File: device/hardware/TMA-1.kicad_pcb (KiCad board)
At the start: 2 copper layers, 143.8 x 129.5 mm, 72 parts, among them J1 MAIN I/O, J2 I2C, Q1 2N3904, Q2 2N3904, Q3 2N3904, Q4 2N3904, Q5 2N3904, Q6 2N3904, Q7 2N3904, Q8 2N3904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

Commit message: improve: pin name silkscreen
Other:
- board text added: "AIN0"
- board text added: "AIN1"
- board text added: "AIN2"
- board text added: "AIN3"
- board text added: "CANH"
- board text added: "CANL"
- board text added: "DIN0"
- board text added: "DIN1"
- board text added: "DIN2"
- board text added: "DIN3"
- board text added: "DIN4"
- board text added: "DIN5"
- board text added: "DIN6"
- board text added: "DIN7"
- board text added: "DRX"
- board text added: "DTX"
- board text added: "GND"
- board text added: "LRX"
- board text added: "LTX"
- board text added: "PIN0"
- board text added: "PIN1"
- board text added: "PIN2"
- board text added: "PIN3"
- board text added: "SCL"
- board text added: "SDA"
- board text added: "VIN"
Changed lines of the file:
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@@
   (gr_line (start 216.408 35.687) (end 216.408 153.035)
     (stroke (width 0.1) (type default)) (layer "Edge.Cuts"))
+  (gr_text "DIN6" (at 175.768 44.577) (layer "B.SilkS")
+    (effects (font (size 1 1) (thickness 0.15)) (justify left bottom mirror))
+  )
+  (gr_text "PIN2" (at 192.532 44.577) (layer "B.SilkS")
+    (effects (font (size 1 1) (thickness 0.15)) (justify left bottom mirror))
+  )
+  (gr_text "PIN1" (at 188.341 56.642) (layer "B.SilkS")
+    (effects (font (size 1 1) (thickness 0.15)) (justify left bottom mirror))
+  )
+  (gr_text "LTX" (at 200.406 44.577) (layer "B.SilkS")
+    (effects (font (size 1 1) (thickness 0.15)) (justify left bottom mirror))
+  )
+  (gr_text "DIN7" (at 175.895 56.642) (layer "B.SilkS")
+    (effects (font (size 1 1) (thickness 0.15)) (justify left bottom mirror))
+  )
+  (gr_text "DIN5" (at 171.577 56.642) (layer "B.SilkS")
+    (effects (font (size 1 1) (thickness 0.15)) (justify left bottom mirror))
+  )
+  (gr_text "DIN1" (at 163.068 56.642) (layer "B.SilkS")
+    (effects (font (size 1 1) (thickness 0.15)) (justify left bottom mirror))
+  )
+  (gr_text "CANL" (at 205.359 56.642) (layer "B.SilkS")
+    (effects (font (size 1 1) (thickness 0.15)) (justify left bottom mirror))
+  )
+  (gr_text "DIN0" (at 163.068 44.577) (layer "B.SilkS")
+    (effects (font (size 1 1) (thickness 0.15)) (justify left bottom mirror))
+  )
+  (gr_text "SDA" (at 211.836 93.472) (layer "B.SilkS")
+    (effects (font (size 1 1) (thickness 0.15)) (justify left bottom mirror))
+  )
+  (gr_text "DRX" (at 196.469 56.642) (layer "B.SilkS")
+    (effects (font (size 1 1) (thickness 0.15)) (justify left bottom mirror))
+  )
+  (gr_text "AIN3" (at 184.15 56.642) (layer "B.SilkS")
+    (effects (font (size 1 1) (thickness 0.15)) (justify left bottom mirror))
+  )
+  (gr_text "AIN2" (at 184.15 44.577) (layer "B.SilkS")
+    (effects (font (size 1 1) (thickness 0.15)) (justify left bottom mirror))
+  )
+  (gr_text "DIN3" (at 167.259 56.642) (layer "B.SilkS")
+    (effects (font (size 1 1) (thickness 0.15)) (justify left bottom mirror))
+  )
+  (gr_text "VIN" (at 158.242 44.577) (layer "B.SilkS")
+    (effects (font (size 1 1) (thickness 0.15)) (justify left bottom mirror))
+  )
+  (gr_text "DIN4" (at 171.577 44.577) (layer "B.SilkS")
+    (effects (font (size 1 1) (thickness 0.15)) (justify left bottom mirror))
+  )
+  (gr_text "DTX" (at 196.469 44.577) (layer "B.SilkS")
+    (effects (font (size 1 1) (thickness 0.15)) (justify left bottom mirror))
+  )
+  (gr_text "GND" (at 158.75 56.642) (layer "B.SilkS")
+    (effects (font (size 1 1) (thickness 0.15)) (justify left bottom mirror))
+  )
+  (gr_text "PIN3" (at 192.532 56.642) (layer "B.SilkS")
+    (effects (font (size 1 1) (thickness 0.15)) (justify left bottom mirror))
+  )
+  (gr_text "DIN2" (at 167.259 44.577) (layer "B.SilkS")
+    (effects (font (size 1 1) (thickness 0.15)) (justify left bottom mirror))
+  )
+  (gr_text "AIN1" (at 179.959 56.642) (layer "B.SilkS")
+    (effects (font (size 1 1) (thickness 0.15)) (justify left bottom mirror))
+  )
+  (gr_text "AIN0" (at 179.959 44.577) (layer "B.SilkS")
+    (effects (font (size 1 1) (thickness 0.15)) (justify left bottom mirror))
+  )
+  (gr_text "CANH" (at 205.359 44.577) (layer "B.SilkS")
+    (effects (font (size 1 1) (thickness 0.15)) (justify left bottom mirror))
+  )
+  (gr_text "LRX" (at 200.533 56.642) (layer "B.SilkS")
+    (effects (font (size 1 1) (thickness 0.15)) (justify left bottom mirror))
+  )
+  (gr_text "SCL" (at 211.836 86.487) (layer "B.SilkS")
+    (effects (font (size 1 1) (thickness 0.15)) (justify left bottom mirror))
+  )
+  (gr_text "PIN0" (at 188.341 44.577) (layer "B.SilkS")
+    (effects (font (size 1 1) (thickness 0.15)) (justify left bottom mirror))
+  )
   (gr_text "PULSE" (at 176.911 146.05) (layer "F.SilkS")
     (effects (font (size 1.27 1.27) (thickness 0.254) bold) (justify left bottom))

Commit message: improve: PCB v1.1 add debug uart jumper
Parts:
- J2: value I2C -> DEBUG UART; footprint Connector_Molex:Molex_SPOX_5267-02A_1x02_P2.50mm_Vertical -> Connector_PinHeader_2.54mm:PinHeader_1x03_P2.54mm_Vertical
- U2: value NodeMCU-32S -> NODEMCU32S
- moved J2 4.03 mm to (210.7, 86.5), turned to 0 degrees
- renumbered C2 to C1
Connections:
- J1 pad 10: /DEBUG_UART_TX -> /LOG_UART_TX
- J1 pad 11: /LOG_UART_TX -> /ESP_I2C_SDA
- J1 pad 22: /DEBUG_UART_RX -> /LOG_UART_RX
- J1 pad 23: /LOG_UART_RX -> /ESP_I2C_SCL
- J2 pad 1: /ESP_I2C_SDA -> /DEBUG_UART_TX
- J2 pad 2: /ESP_I2C_SCL -> /DEBUG_UART_RX
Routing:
- net /DEBUG_UART_RX: track 190.2 -> 233.4 mm
- net /ESP_I2C_SDA: track 222.0 -> 264.8 mm
- net /DEBUG_UART_TX: track 174.9 -> 217.4 mm
- net /ESP_I2C_SCL: track 216.1 -> 248.7 mm
- net /LOG_UART_RX: track 198.1 -> 196.2 mm
- net /LOG_UART_TX: track 191.8 -> 190.0 mm
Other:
- board text added: "Monolith TMA-1 Datalogger v1.1"
- board text added: "RX"
- board text added: "TX"
- board text removed: "DRX"
- board text removed: "DTX"
- board text removed: "Monolith TMA-1 Datalogger v1.0"

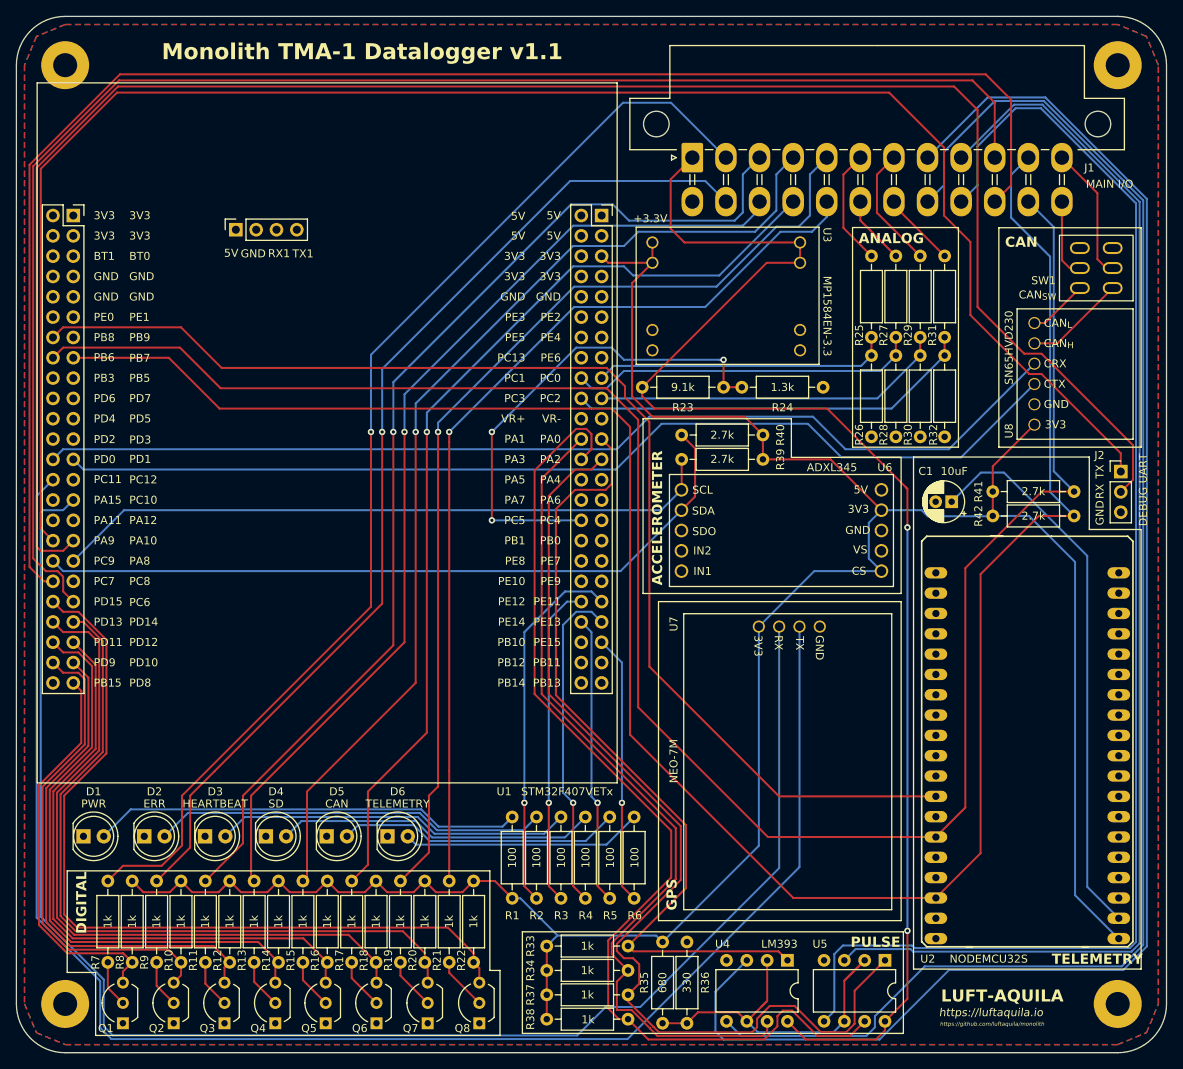
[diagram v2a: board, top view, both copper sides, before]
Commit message: fix: misc bugs PCB v1.2
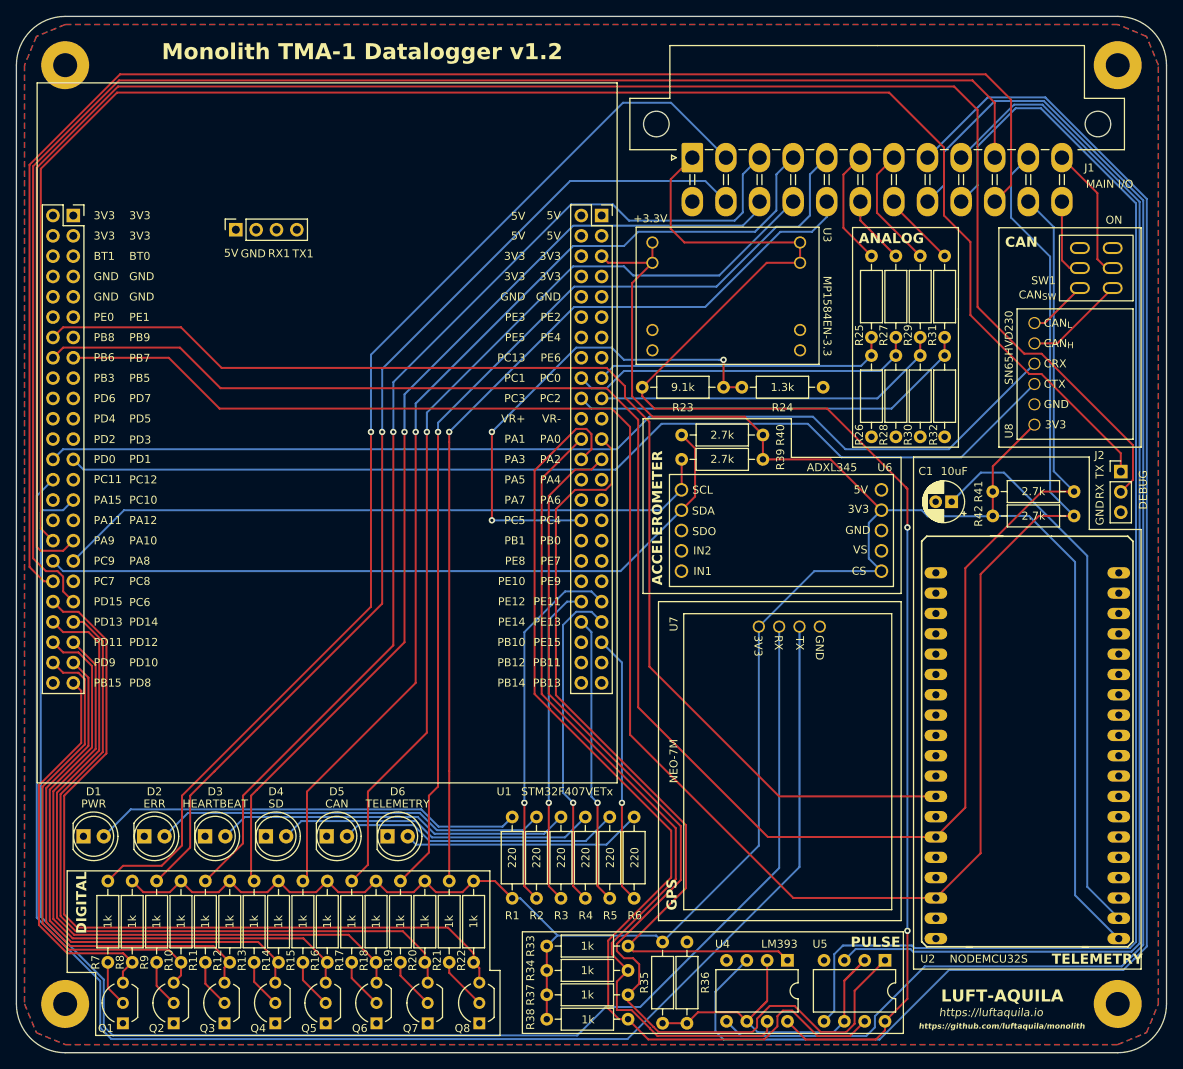
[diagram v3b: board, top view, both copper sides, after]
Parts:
- J2: value DEBUG UART -> DEBUG
- R1, R2, R3, R4, R5, R6: value 100 -> 220
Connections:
- U2 pad GND@2: unconnected-(U2-PadGND@2) -> GND
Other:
- board text added: "Monolith TMA-1 Datalogger v1.2"
- board text added: "ON"
- board text removed: "Monolith TMA-1 Datalogger v1.1"
